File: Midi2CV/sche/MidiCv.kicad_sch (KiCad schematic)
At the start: 21 parts, among them J3 Conn_01x01_Pin, J4 Conn_01x01_Pin, J5 Conn_01x01_Pin, Q1 2N7000, U1 STM32F103C8T6_BD, U2 6N138, U4 MCP4725xxx-xCH

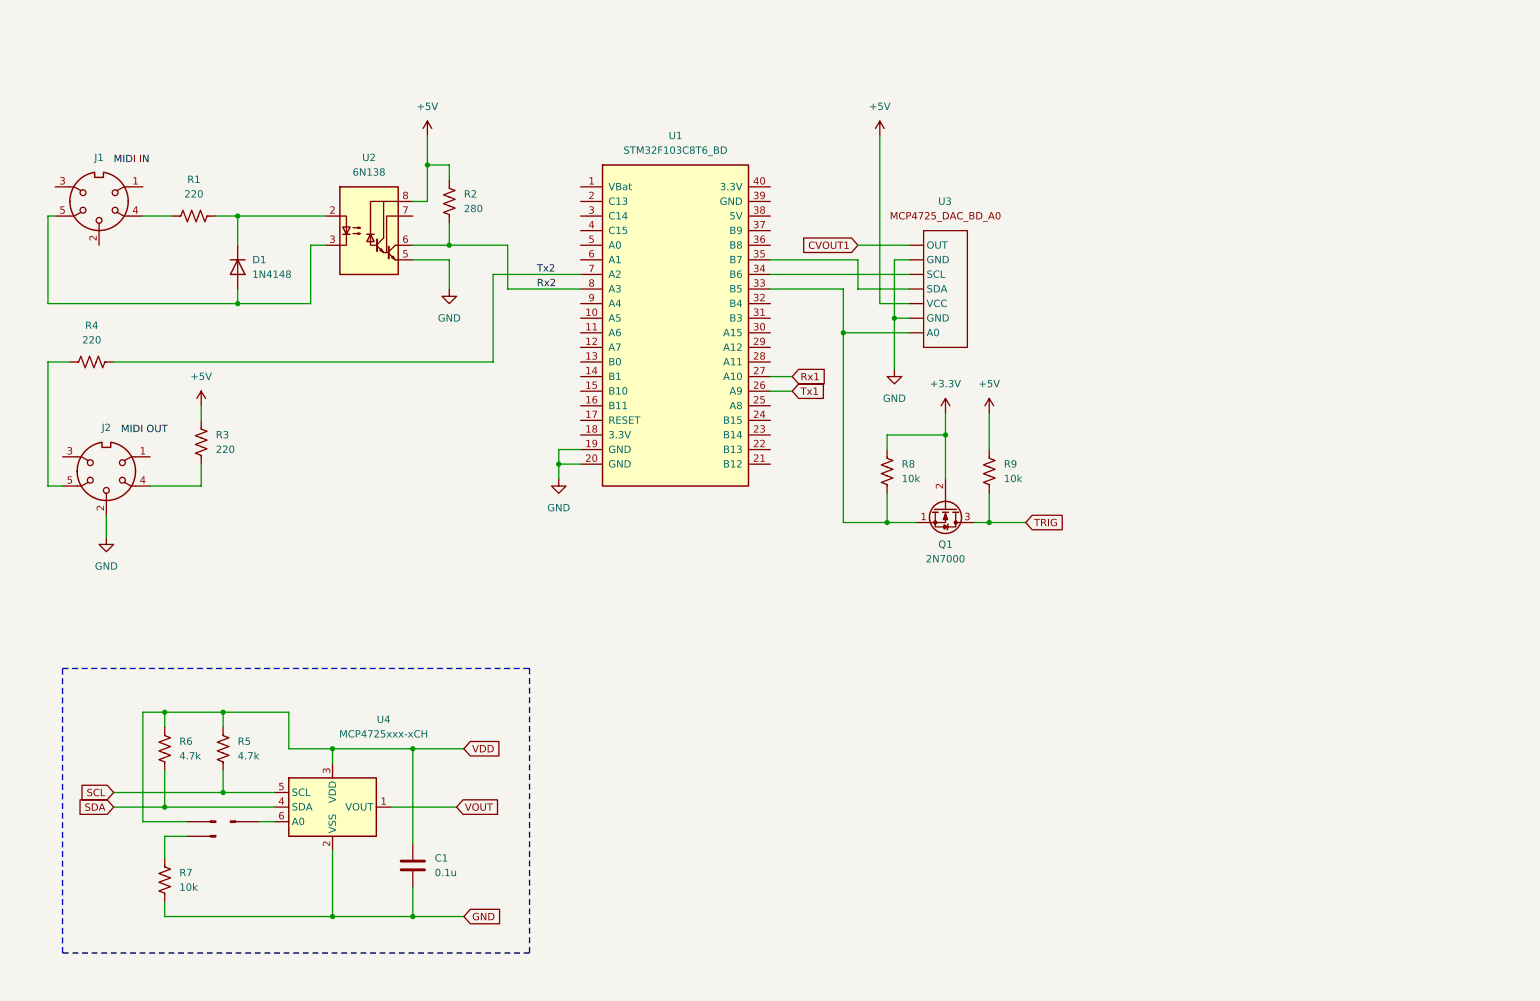
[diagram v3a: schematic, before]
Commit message: add DAC control, 8ch CV schematic
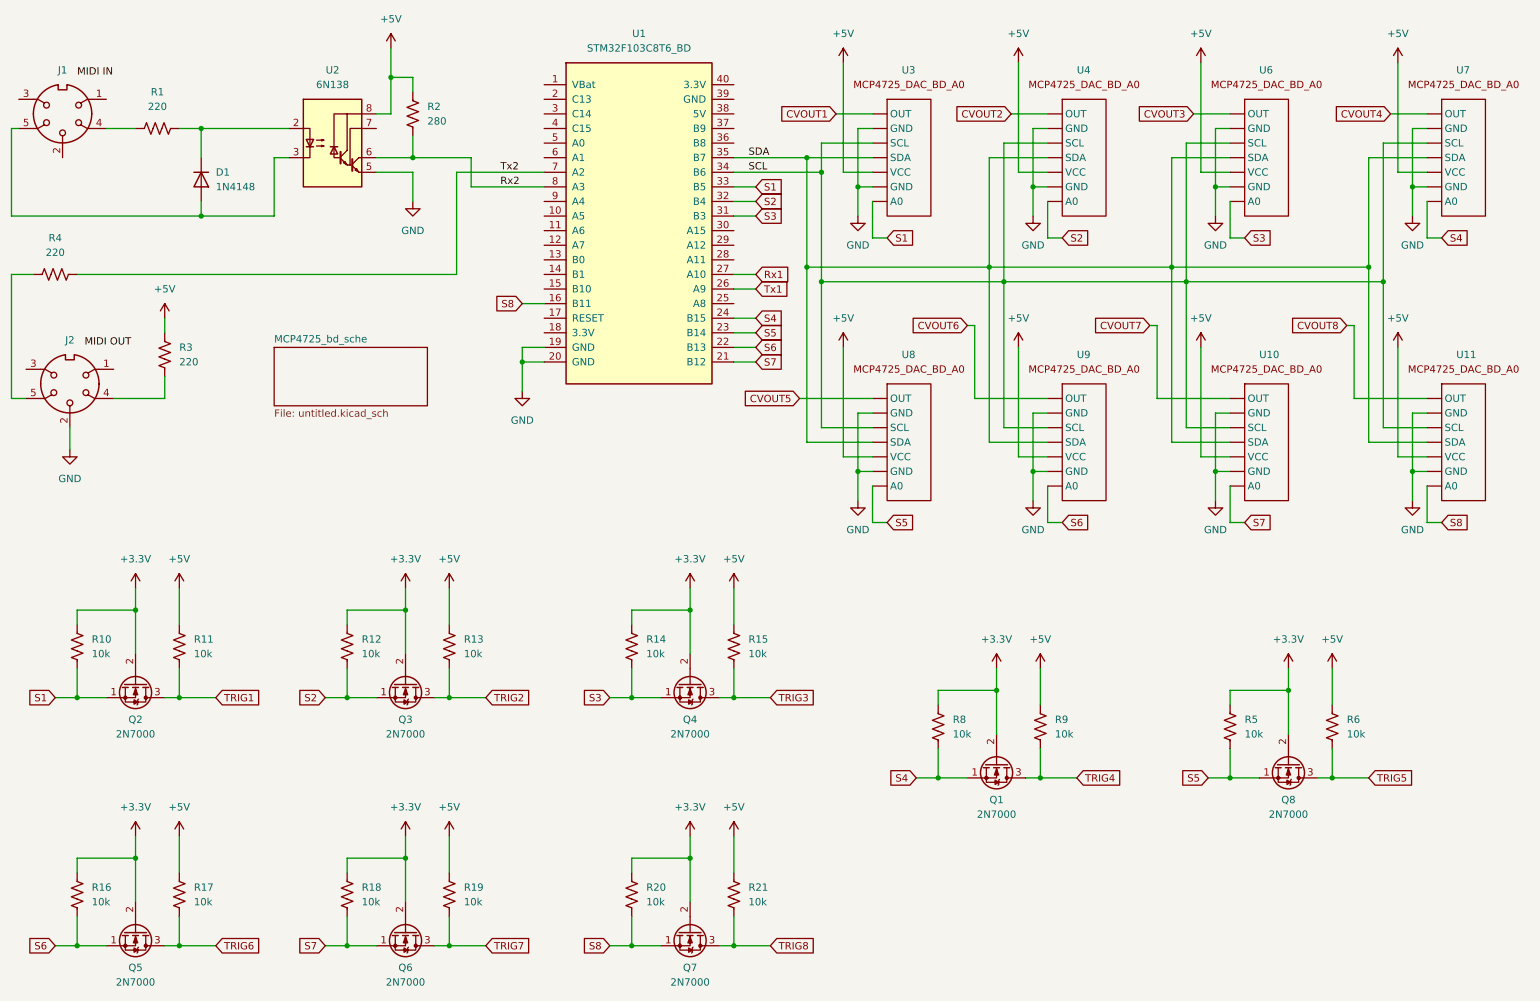
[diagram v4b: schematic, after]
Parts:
- removed C1: 0.1u, symbol Device:C
- removed J3, J4, J5: Conn_01x01_Pin, symbol Connector:Conn_01x01_Pin
- removed R7: 10k, symbol Device:R_US
- removed U4: MCP4725xxx-xCH, Package_TO_SOT_SMD:SOT-23-6, symbol Analog_DAC:MCP4725xxx-xCH
- added Q2, Q3, Q4, Q5, Q6, Q7, Q8: 2N7000, Package_TO_SOT_THT:TO-92_Inline, symbol Transistor_FET:2N7000
- added R10, R11, R12, R13, R14, R15, R16, R17, R18, R19, R20, R21: 10k, symbol Device:R_US
- added U10, U11, U4, U6, U7, U8, U9: ~, symbol RetroElec:MCP4725_DAC_BD_A0
- R5, R6: value 4.7k -> 10k
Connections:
- net +3.3V: now also R5.2, Q2.2 (G), Q3.2 (G), Q4.2 (G), Q5.2 (G), Q6.2 (G), Q7.2 (G), Q8.2 (G), R10.2, R12.2, R14.2, R16.2, R18.2, R20.2
- net +5V: now also R6.2, R11.2, R13.2, R15.2, R17.2, R19.2, R21.2, U10. (VCC), U11. (VCC), U4. (VCC), U6. (VCC), U7. (VCC), U8. (VCC), U9. (VCC)
- net GND: now also U10. (VCC), U11. (VCC), U4. (VCC), U6. (VCC), U7. (VCC), U8. (VCC), U9. (VCC)
- net SCL: now also U1.34 (B6), U3. (VCC), U10. (VCC), U11. (VCC), U4. (VCC), U6. (VCC), U7. (VCC), U8. (VCC), U9. (VCC); no longer R5.1
- net SDA: now also U1.35 (B7), U3. (VCC), U10. (VCC), U11. (VCC), U4. (VCC), U6. (VCC), U7. (VCC), U8. (VCC), U9. (VCC); no longer R6.1
- net S4: now reaches Q1.1 (S), R8.1
- net S4: now also U1.24 (B15), U7. (VCC); no longer U1.33 (B5), U3. (VCC)
- net S8: now reaches U1.16 (B11)
- net S8: now also Q7.1 (S), R20.1, U11. (VCC)
- net S7: now reaches U1.21 (B12)
- net S7: now also Q6.1 (S), R18.1, U10. (VCC)
- net S6: now reaches U1.22 (B13)
- net S6: now also Q5.1 (S), R16.1, U9. (VCC)
- net S5: now reaches U1.23 (B14)
- net S5: now also R5.1, Q8.1 (S), U8. (VCC)
- net S3: now reaches U1.31 (B3)
- net S3: now also Q4.1 (S), R14.1, U6. (VCC)
- net S2: now reaches U1.32 (B4)
- net S2: now also Q3.1 (S), R12.1, U4. (VCC)
- net TRIG renamed TRIG4
- removed net VDD: R5.2, R6.2
- new net CVOUT2: U4. (VCC)
- new net CVOUT3: U6. (VCC)
- new net CVOUT4: U7. (VCC)
- new net CVOUT5: U8. (VCC)
- new net CVOUT6: U9. (VCC)
- new net CVOUT7: U10. (VCC)
- new net CVOUT8: U11. (VCC)
- new net S1: Q2.1 (S), R10.1, U1.33 (B5), U3. (VCC)
- new net TRIG1: Q2.3 (D), R11.1
- new net TRIG2: Q3.3 (D), R13.1
- new net TRIG3: Q4.3 (D), R15.1
- new net TRIG5: Q8.3 (D), R6.1
- new net TRIG6: Q5.3 (D), R17.1
- new net TRIG7: Q6.3 (D), R19.1
- new net TRIG8: Q7.3 (D), R21.1
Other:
- added sheet MCP4725_bd_sche (untitled.kicad_sch)
- moved on the sheet: D1, J1, J2, Q1, R1, R2, R3, R4, R8, R9, U1, U2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

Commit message: update midi2cv schematic
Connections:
- net S8: now also U1.14 (B1); no longer U1.16 (B11)
- net SCL2: now reaches U1.15 (B10)
- new net SDA2: U1.16 (B11)
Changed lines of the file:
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@@
+    (stroke (width 0) (type default))
+  )
+  (wire (pts (xy 107.95 71.12) (xy 111.76 71.12))
     (stroke (width 0) (type default))
   )
@@
     (stroke (width 0) (type default))
   )
+  (wire (pts (xy 107.95 66.04) (xy 111.76 66.04))
+    (stroke (width 0) (type default))
+  )
   (wire (pts (xy 226.06 29.21) (xy 226.06 48.26))
     (stroke (width 0) (type default))
@@
     (stroke (width 0) (type default))
   )
-  (wire (pts (xy 107.95 71.12) (xy 111.76 71.12))
-    (stroke (width 0) (type default))
-  )
   (wire (pts (xy 19.05 55.88) (xy 52.07 55.88))
     (stroke (width 0) (type default))
@@
   )
   (wire (pts (xy 88.9 45.72) (xy 99.06 45.72))
+    (stroke (width 0) (type default))
+  )
+  (wire (pts (xy 107.95 68.58) (xy 111.76 68.58))
     (stroke (width 0) (type default))
   )
@@
     )
   )
-  (global_label "S8" (shape input) (at 107.95 71.12 180) (fields_autoplaced)
-    (effects (font (size 1.27 1.27)) (justify right))
-    (property "Intersheetrefs" "${INTERSHEET_REFS}" (at 102.5458 71.12 0)
+  (global_label "S8" (shape input) (at 107.95 66.04 180) (fields_autoplaced)
+    (effects (font (size 1.27 1.27)) (justify right))
+    (property "Intersheetrefs" "${INTERSHEET_REFS}" (at 102.5458 66.04 0)
       (effects (font (size 1.27 1.27)) (justify right) hide)
     )
@@
     )
   )
+  (global_label "SCL2" (shape input) (at 107.95 68.58 180) (fields_autoplaced)
+    (effects (font (size 1.27 1.27)) (justify right))
+    (property "Intersheetrefs" "${INTERSHEET_REFS}" (at 100.2477 68.58 0)
+      (effects (font (size 1.27 1.27)) (justify right) hide)
+    )
+  )
   (global_label "S8" (shape input) (at 267.97 109.22 0) (fields_autoplaced)
     (effects (font (size 1.27 1.27)) (justify left))
@@
       (effects (font (size 1.27 1.27)) (justify right) hide)
     )
+  )
+  (global_label "SDA2" (shape input) (at 107.95 71.12 180) (fields_autoplaced)
+    (effects (font (size 1.27 1.27)) (justify right))
+    (property "Intersheetrefs" "${INTERSHEET_REFS}" (at 100.1872 71.12 0)
+      (effects (font (size 1.27 1.27)) (justify right) hide)
+    )
